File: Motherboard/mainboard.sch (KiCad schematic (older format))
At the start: 48 parts, among them IC1 BMX160, J1 Conn_01x01, J2 10118194-0001LF, J28 Conn_01x01, J29 Conn_01x01, J3 Micro_SD_Card, J30 Conn_01x01, J4 xf2m-2415-1a, J5 XF2M-1015-1A, SW1 KMR231NG LFS, U1 RFM95W-915S2, U2 ATSAMD51G_TQFN48, U4 TPS82740BSIPR, U6 MAX708RESA-T, U8 RFM95W-915S2, X1 ANTENNA_U.FL, X2 ANTENNA_U.FL

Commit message: updated PCB layout
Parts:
- C1, C2, C3, C4, C5, C7, C8: symbol Device:C_Small -> mainboard-rescue:C_Small-Device
- C10, C14: renamed from C?; value C -> 10uF; footprint (none) -> Capacitor_SMD:C_0402_1005Metric; symbol Device:C -> mainboard-rescue:C-Device
- C11, C13: renamed from C?; value C -> 2.2uF; footprint (none) -> Capacitor_SMD:C_0402_1005Metric; symbol Device:C -> mainboard-rescue:C-Device
- C12, C9: renamed from C?; value C -> 0.1uF; footprint (none) -> Capacitor_SMD:C_0402_1005Metric; symbol Device:C -> mainboard-rescue:C-Device
- D2: symbol Device:D_Schottky -> mainboard-rescue:D_Schottky-Device
- J1, J28, J29, J30: symbol Connector_Generic:Conn_01x01 -> mainboard-rescue:Conn_01x01-Connector_Generic
- L1: symbol Device:L_Small -> mainboard-rescue:L_Small-Device
- R1, R2, R3, R5: symbol Device:R_US -> mainboard-rescue:R_US-Device
- R4, R6, R7, R8: renamed from R?; symbol Device:R_US -> mainboard-rescue:R_US-Device
- U3: renamed from U?; symbol Driver_Motor:DRV8848 -> mainboard-rescue:DRV8848-Driver_Motor
- U5: renamed from U?; footprint Package_SO:TSSOP-16-1EP_4.4x5mm_P0.65mm -> KiCAD Libraries:SOP65P640X120-17N; symbol Driver_Motor:DRV8848 -> mainboard-rescue:DRV8848-Driver_Motor
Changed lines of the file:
@@
 	900  5500 1450 5500
 $Comp
-L Device:R_US R1
+L mainboard-rescue:R_US-Device R1
 U 1 1 5C3B885A
 P 900 5650
@@
 $EndComp
 $Comp
-L Device:R_US R5
+L mainboard-rescue:R_US-Device R5
 U 1 1 5C6310F9
 P 5150 7200
@@
 Connection ~ 1150 4100
 $Comp
-L Device:R_US R2
+L mainboard-rescue:R_US-Device R2
 U 1 1 5C6E5301
 P 1150 3950
@@
 SAMD51\n
 $Comp
-L Device:L_Small L1
+L mainboard-rescue:L_Small-Device L1
 U 1 1 5C59C1B4
 P 1350 4800
@@
 UHF RADIO\n
 $Comp
-L Device:C_Small C1
+L mainboard-rescue:C_Small-Device C1
 U 1 1 5DA4F94A
 P 750 6850
@@
 $EndComp
 $Comp
-L Device:C_Small C7
+L mainboard-rescue:C_Small-Device C7
 U 1 1 5DA4FC48
 P 1150 6850
@@
 Connection ~ 5700 5550
 $Comp
-L Device:D_Schottky D2
+L mainboard-rescue:D_Schottky-Device D2
 U 1 1 5D1876FB
 P 5550 4750
@@
 Connection ~ 5700 4750
 $Comp
-L Device:C_Small C2
+L mainboard-rescue:C_Small-Device C2
 U 1 1 5D1BA86A
 P 800 4800
@@
 $EndComp
 $Comp
-L Device:C_Small C5
+L mainboard-rescue:C_Small-Device C5
 U 1 1 5D1BB024
 P 1000 4800
@@
 	1000 4700 1250 4700
 $Comp
-L Device:C_Small C3
+L mainboard-rescue:C_Small-Device C3
 U 1 1 5D1C3FDB
 P 950 6850
@@
 PA07
 $Comp
-L Connector_Generic:Conn_01x01 J28
+L mainboard-rescue:Conn_01x01-Connector_Generic J28
 U 1 1 5D2A6718
 P 5000 7550
@@
 $EndComp
 $Comp
-L Connector_Generic:Conn_01x01 J1
+L mainboard-rescue:Conn_01x01-Connector_Generic J1
 U 1 1 5D2B62DF
 P 4900 7550
@@
 $EndComp
 $Comp
-L Connector_Generic:Conn_01x01 J29
+L mainboard-rescue:Conn_01x01-Connector_Generic J29
 U 1 1 5D32C3EB
 P 4800 7550
@@
 $EndComp
 $Comp
-L Connector_Generic:Conn_01x01 J30
+L mainboard-rescue:Conn_01x01-Connector_Generic J30
 U 1 1 5D338152
 P 5100 7550
@@
 $EndComp
 $Comp
-L Device:R_US R3
+L mainboard-rescue:R_US-Device R3
 U 1 1 5DAB9E18
 P 3050 1600
@@
 NoConn ~ 3300 1250
 $Comp
-L Device:C_Small C4
+L mainboard-rescue:C_Small-Device C4
 U 1 1 5DAEE375
 P 1100 1500
@@
 	1100 1600 750  1600
 $Comp
-L Device:C_Small C8
+L mainboard-rescue:C_Small-Device C8
 U 1 1 5DAF534D
 P 2700 1100
@@
 	5350 7000 5350 7350
 $Comp
-L Device:C C?
+L mainboard-rescue:C-Device C9
 U 1 1 5DB69DAC
 P 8050 900
-F 0 "C?" H 8165 946 50  0000 L CNN
-F 1 "C" H 8165 855 50  0000 L CNN
-F 2 "" H 8088 750 50  0001 C CNN
+F 0 "C9" H 8165 946 50  0000 L CNN
+F 1 "0.1uF" H 8165 855 50  0000 L CNN
+F 2 "Capacitor_SMD:C_0402_1005Metric" H 8088 750 50  0001 C CNN
 F 3 "~" H 8050 900 50  0001 C CNN
 	1    8050 900
@@
 $EndComp
 $Comp
-L Device:C C?
+L mainboard-rescue:C-Device C10
 U 1 1 5DB6B170
 P 8400 900
-F 0 "C?" H 8515 946 50  0000 L CNN
-F 1 "C" H 8515 855 50  0000 L CNN
-F 2 "" H 8438 750 50  0001 C CNN
+F 0 "C10" H 8515 946 50  0000 L CNN
+F 1 "10uF" H 8515 855 50  0000 L CNN
+F 2 "Capacitor_SMD:C_0402_1005Metric" H 8438 750 50  0001 C CNN
 F 3 "~" H 8400 900 50  0001 C CNN
 	1    8400 900
@@
 $EndComp
 $Comp
-L Device:C C?
+L mainboard-rescue:C-Device C11
 U 1 1 5DB6BC2C
 P 8150 1200
-F 0 "C?" H 8265 1246 50  0000 L CNN
-F 1 "C" H 8265 1155 50  0000 L CNN
-F 2 "" H 8188 1050 50  0001 C CNN
+F 0 "C11" H 8265 1246 50  0000 L CNN
+F 1 "2.2uF" H 8265 1155 50  0000 L CNN
+F 2 "Capacitor_SMD:C_0402_1005Metric" H 8188 1050 50  0001 C CNN
 F 3 "~" H 8150 1200 50  0001 C CNN
 	1    8150 1200
@@
 	8050 750  8400 750
 $Comp
-L power:GND #PWR?
+L power:GND #PWR0124
 U 1 1 5DBF1F8E
 P 8400 1050
-F 0 "#PWR?" H 8400 800 50  0001 C CNN
+F 0 "#PWR0124" H 8400 800 50  0001 C CNN
 F 1 "GND" H 8405 877 50  0000 C CNN
 F 2 "" H 8400 1050 50  0001 C CNN
@@
 	7500 750  8050 750
 $Comp
-L power:GND #PWR?
+L power:GND #PWR0125
 U 1 1 5DC582A1
 P 7500 2550
-F 0 "#PWR?" H 7500 2300 50  0001 C CNN
+F 0 "#PWR0125" H 7500 2300 50  0001 C CNN
 F 1 "GND" H 7505 2377 50  0000 C CNN
 F 2 "" H 7500 2550 50  0001 C CNN
@@
 MINZ_2
 $Comp
-L Driver_Motor:DRV8848 U?
+L mainboard-rescue:DRV8848-Driver_Motor U3
 U 1 1 5DB469CF
 P 7500 1850
-F 0 "U?" H 7500 2631 50  0000 C CNN
+F 0 "U3" H 7500 2631 50  0000 C CNN
 F 1 "DRV8848" H 7500 2540 50  0000 C CNN
 F 2 "Package_SO:TSSOP-16-1EP_4.4x5mm_P0.65mm" H 7500 1150 50  0001 C CNN
@@
 Connection ~ 7500 2450
 $Comp
-L power:GND #PWR?
+L power:GND #PWR0128
 U 1 1 5DCE2BBF
 P 8100 1850
-F 0 "#PWR?" H 8100 1600 50  0001 C CNN
+F 0 "#PWR0128" H 8100 1600 50  0001 C CNN
 F 1 "GND" H 8105 1677 50  0000 C CNN
 F 2 "" H 8100 1850 50  0001 C CNN
@@
 $EndComp
 $Comp
-L power:GND #PWR?
+L power:GND #PWR0129
 U 1 1 5DCE9737
 P 8100 2250
-F 0 "#PWR?" H 8100 2000 50  0001 C CNN
+F 0 "#PWR0129" H 8100 2000 50  0001 C CNN
 F 1 "GND" H 8105 2077 50  0000 C CNN
 F 2 "" H 8100 2250 50  0001 C CNN
@@
 $EndComp
 $Comp
-L Device:C C?
+L mainboard-rescue:C-Device C12
 U 1 1 5DD0AEB4
 P 9950 850
-F 0 "C?" H 10065 896 50  0000 L CNN
-F 1 "C" H 10065 805 50  0000 L CNN
-F 2 "" H 9988 700 50  0001 C CNN
+F 0 "C12" H 10065 896 50  0000 L CNN
+F 1 "0.1uF" H 10065 805 50  0000 L CNN
+F 2 "Capacitor_SMD:C_0402_1005Metric" H 9988 700 50  0001 C CNN
 F 3 "~" H 9950 850 50  0001 C CNN
 	1    9950 850
@@
 $EndComp
 $Comp
-L Device:C C?
+L mainboard-rescue:C-Device C14
 U 1 1 5DD0AEBA
 P 10300 850
-F 0 "C?" H 10415 896 50  0000 L CNN
-F 1 "C" H 10415 805 50  0000 L CNN
-F 2 "" H 10338 700 50  0001 C CNN
+F 0 "C14" H 10415 896 50  0000 L CNN
+F 1 "10uF" H 10415 805 50  0000 L CNN
+F 2 "Capacitor_SMD:C_0402_1005Metric" H 10338 700 50  0001 C CNN
 F 3 "~" H 10300 850 50  0001 C CNN
 	1    10300 850
@@
 $EndComp
 $Comp
-L Device:C C?
+L mainboard-rescue:C-Device C13
 U 1 1 5DD0AEC0
 P 10050 1150
-F 0 "C?" H 10165 1196 50  0000 L CNN
-F 1 "C" H 10165 1105 50  0000 L CNN
-F 2 "" H 10088 1000 50  0001 C CNN
+F 0 "C13" H 10165 1196 50  0000 L CNN
+F 1 "2.2uF" H 10165 1105 50  0000 L CNN
+F 2 "Capacitor_SMD:C_0402_1005Metric" H 10088 1000 50  0001 C CNN
 F 3 "~" H 10050 1150 50  0001 C CNN
 	1    10050 1150
@@
 	9950 700  10300 700
 $Comp
-L power:GND #PWR?
+L power:GND #PWR0130
 U 1 1 5DD0AEC8
 P 10300 1000
-F 0 "#PWR?" H 10300 750 50  0001 C CNN
+F 0 "#PWR0130" H 10300 750 50  0001 C CNN
 F 1 "GND" H 10305 827 50  0000 C CNN
 F 2 "" H 10300 1000 50  0001 C CNN
@@
 	9400 700  9950 700
 $Comp
-L power:GND #PWR?
+L power:GND #PWR0131
 U 1 1 5DD0AED6
 P 9400 2500
-F 0 "#PWR?" H 9400 2250 50  0001 C CNN
+F 0 "#PWR0131" H 9400 2250 50  0001 C CNN
 F 1 "GND" H 9405 2327 50  0000 C CNN
 F 2 "" H 9400 2500 50  0001 C CNN
@@
 MINZ_2
 $Comp
-L Driver_Motor:DRV8848 U?
+L mainboard-rescue:DRV8848-Driver_Motor U5
 U 1 1 5DD0AEE3
 P 9400 1800
-F 0 "U?" H 9400 2581 50  0000 C CNN
+F 0 "U5" H 9400 2581 50  0000 C CNN
 F 1 "DRV8848" H 9400 2490 50  0000 C CNN
-F 2 "Package_SO:TSSOP-16-1EP_4.4x5mm_P0.65mm" H 9400 1100 50  0001 C CNN
+F 2 "KiCAD Libraries:SOP65P640X120-17N" H 9400 1100 50  0001 C CNN
 F 3 "http://www.ti.com/lit/ds/symlink/drv8848.pdf" H 8250 3150 50  0001 C CNN
 	1    9400 1800
@@
 Connection ~ 9400 2400
 $Comp
-L power:GND #PWR?
+L power:GND #PWR0132
 U 1 1 5DD0AEF2
 P 10000 1800
-F 0 "#PWR?" H 10000 1550 50  0001 C CNN
+F 0 "#PWR0132" H 10000 1550 50  0001 C CNN
 F 1 "GND" H 10005 1627 50  0000 C CNN
 F 2 "" H 10000 1800 50  0001 C CNN
@@
 	10000 1850 10000 1800
 $Comp
-L power:GND #PWR?
+L power:GND #PWR0133
 U 1 1 5DD0AEF9
 P 10000 2200
-F 0 "#PWR?" H 10000 1950 50  0001 C CNN
+F 0 "#PWR0133" H 10000 1950 50  0001 C CNN
 F 1 "GND" H 10005 2027 50  0000 C CNN
 F 2 "" H 10000 2200 50  0001 C CNN
@@
 	4550 6200 4450 6200
 $Comp
-L Device:R_US R?
+L mainboard-rescue:R_US-Device R4
 U 1 1 5DB0C8A9
 P 4500 3950
-F 0 "R?" H 4600 3750 50  0000 C CNN
+F 0 "R4" H 4600 3750 50  0000 C CNN
 F 1 "10K" H 4600 3850 50  0000 C CNN
 F 2 "Resistor_SMD:R_0402_1005Metric" V 4540 3940 50  0001 C CNN
@@
 	4500 4100 4450 4100
 $Comp
-L Device:R_US R?
+L mainboard-rescue:R_US-Device R6
 U 1 1 5DB0D4A3
 P 4650 3850
-F 0 "R?" H 4550 3800 50  0000 C CNN
+F 0 "R6" H 4550 3800 50  0000 C CNN
 F 1 "10K" H 4550 3900 50  0000 C CNN
 F 2 "Resistor_SMD:R_0402_1005Metric" V 4690 3840 50  0001 C CNN
@@
 	4650 4000 4700 4000
 $Comp
-L power:+3V3 #PWR?
+L power:+3V3 #PWR0134
 U 1 1 5DB0E5CD
 P 4650 3600
-F 0 "#PWR?" H 4650 3450 50  0001 C CNN
+F 0 "#PWR0134" H 4650 3450 50  0001 C CNN
 F 1 "+3V3" H 4665 3773 50  0000 C CNN
 F 2 "" H 4650 3600 50  0001 C CNN
@@
 NoConn ~ 1150 2200
 $Comp
-L Device:R_US R?
+L mainboard-rescue:R_US-Device R7
 U 1 1 5DB33981
 P 5100 5750
-F 0 "R?" H 5200 5550 50  0000 C CNN
+F 0 "R7" H 5200 5550 50  0000 C CNN
 F 1 "10K" H 5200 5650 50  0000 C CNN
 F 2 "Resistor_SMD:R_0402_1005Metric" V 5140 5740 50  0001 C CNN
@@
 $EndComp
 $Comp
-L Device:R_US R?
+L mainboard-rescue:R_US-Device R8
 U 1 1 5DB33987
 P 5250 5650
-F 0 "R?" H 5150 5600 50  0000 C CNN
+F 0 "R8" H 5150 5600 50  0000 C CNN
 F 1 "10K" H 5150 5700 50  0000 C CNN
 F 2 "Resistor_SMD:R_0402_1005Metric" V 5290 5640 50  0001 C CNN
@@
 $EndComp
 $Comp
-L power:+3V3 #PWR?
+L power:+3V3 #PWR0135
 U 1 1 5DB3398D
 P 5250 5400
-F 0 "#PWR?" H 5250 5250 50  0001 C CNN
+F 0 "#PWR0135" H 5250 5250 50  0001 C CNN
 F 1 "+3V3" H 5265 5573 50  0000 C CNN
 F 2 "" H 5250 5400 50  0001 C CNN

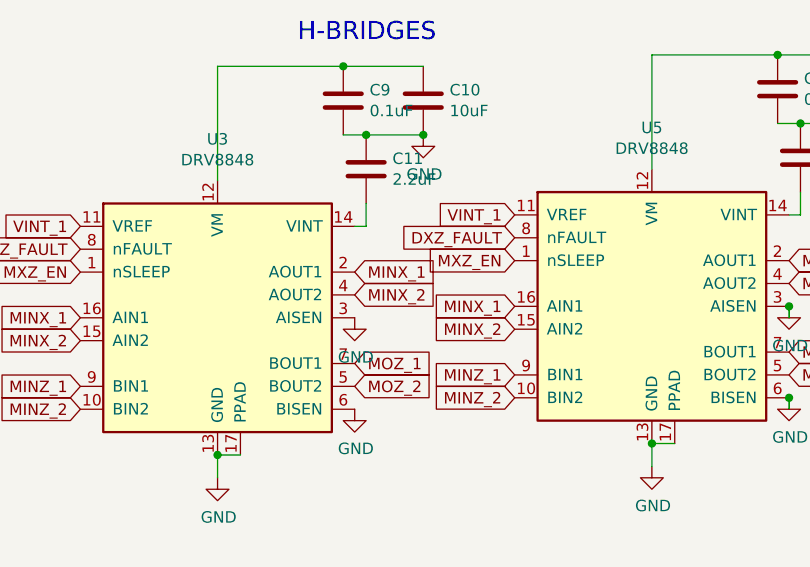
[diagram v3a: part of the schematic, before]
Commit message: updated H-bridge nets on schematic
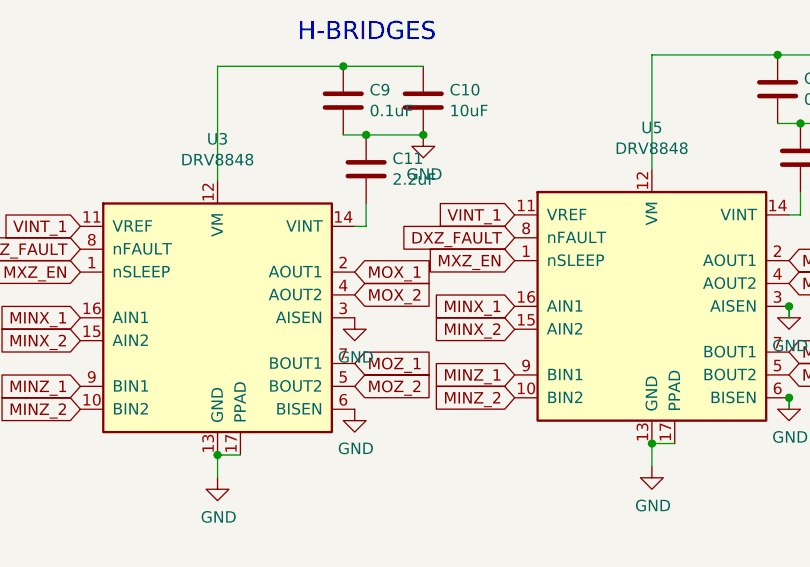
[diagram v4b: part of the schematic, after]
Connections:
- net MINX_1: no longer U3.2 (AOUT1)
- net MINX_2: no longer U3.4 (AOUT2)
- new net MOX_1: U3.2 (AOUT1)
- new net MOX_2: U3.4 (AOUT2)
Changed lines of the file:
@@
 $EndComp
 Text GLabel 8100 1650 2    50   Input ~ 0
-MINX_1
+MOX_1
 Text GLabel 8100 1750 2    50   Input ~ 0
-MINX_2
+MOX_2
 Text GLabel 8100 2050 2    50   Input ~ 0
 MOZ_1

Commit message: updated H-bridge footprints with footprints from component search engine
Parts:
- U3: footprint Package_SO:TSSOP-16-1EP_4.4x5mm_P0.65mm -> KiCAD Libraries:SOP65P640X120-17N
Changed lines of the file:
@@
 F 0 "U3" H 7500 2631 50  0000 C CNN
 F 1 "DRV8848" H 7500 2540 50  0000 C CNN
-F 2 "Package_SO:TSSOP-16-1EP_4.4x5mm_P0.65mm" H 7500 1150 50  0001 C CNN
+F 2 "KiCAD Libraries:SOP65P640X120-17N" H 7500 1150 50  0001 C CNN
 F 3 "http://www.ti.com/lit/ds/symlink/drv8848.pdf" H 6350 3200 50  0001 C CNN
 	1    7500 1850

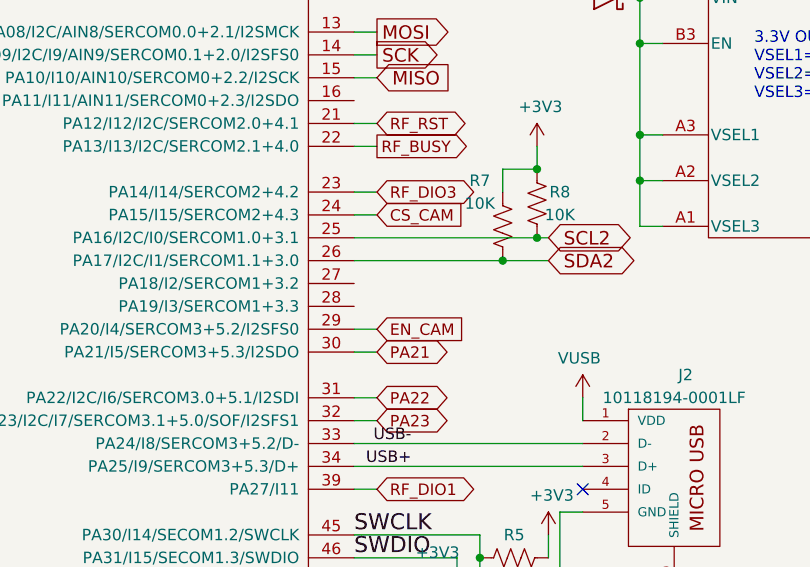
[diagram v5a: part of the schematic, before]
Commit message: updated wiring on top layer, added CS_IMU net
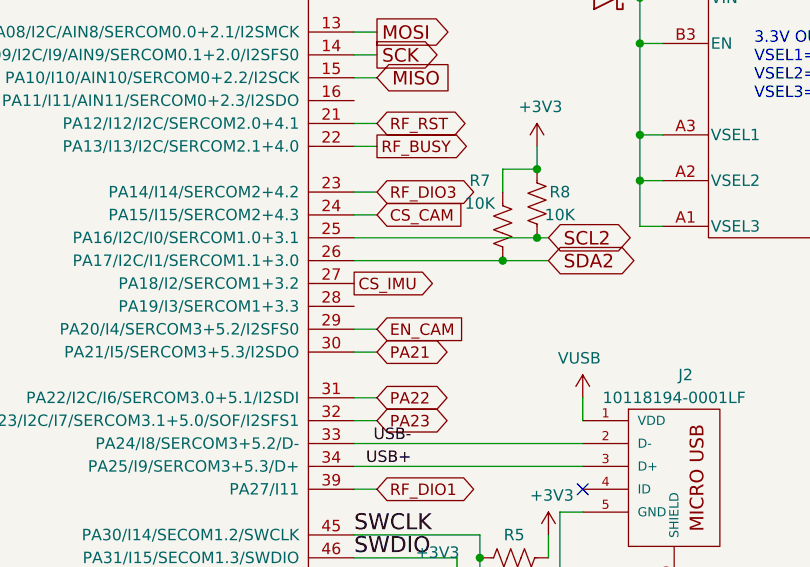
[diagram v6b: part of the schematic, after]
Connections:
- net CS_IMU: now also U2.27 (PA18/I2/SERCOM1+3.2)
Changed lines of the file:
@@
 Wire Wire Line
 	5250 5800 5300 5800
+Text GLabel 4450 6000 2    50   Output ~ 0
+CS_IMU
 $EndSCHEMATC

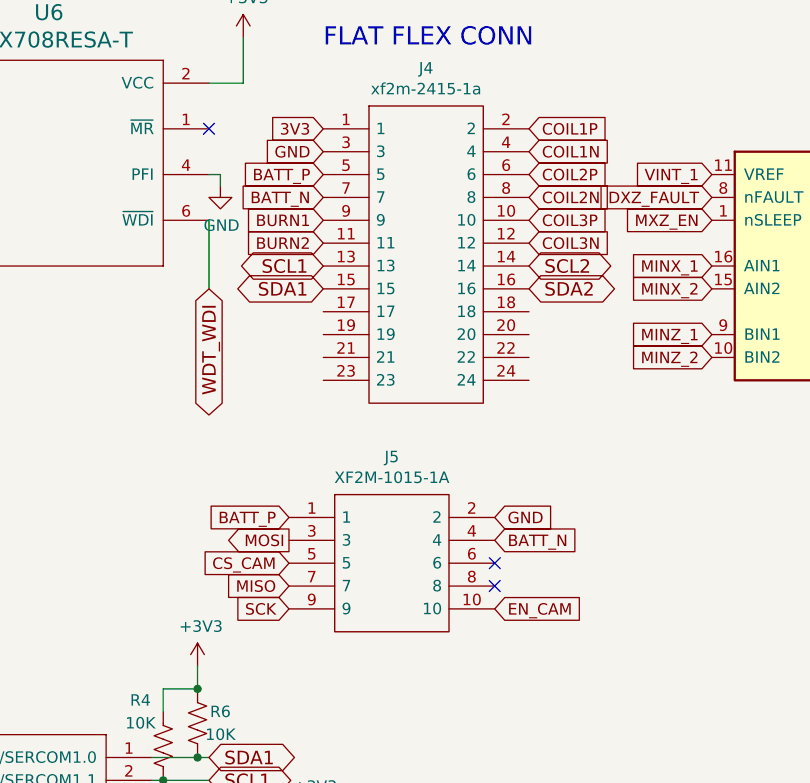
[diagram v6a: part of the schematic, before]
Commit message: updated camera connector and connected to MCU and flat flex connector
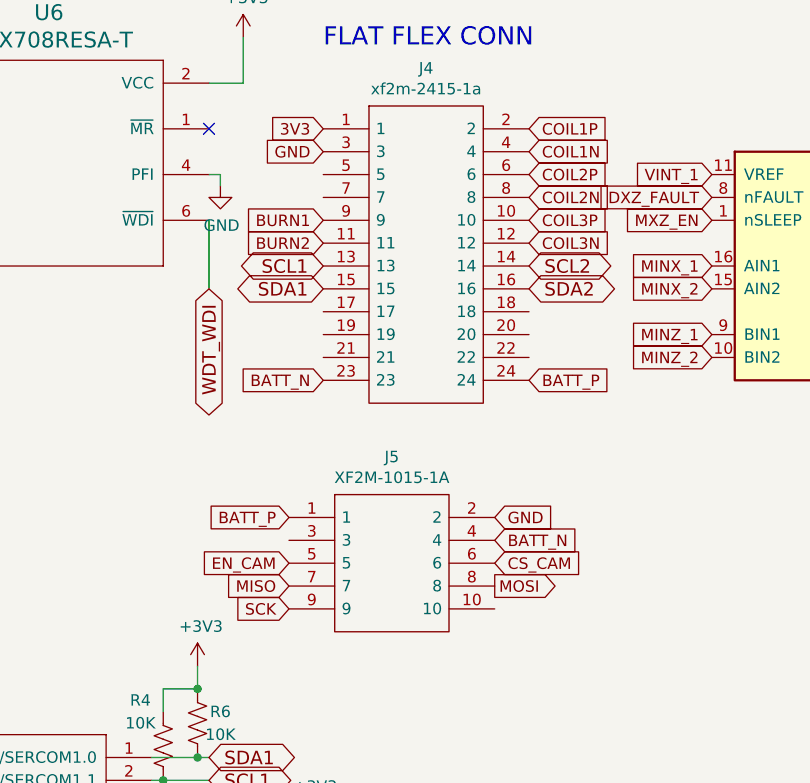
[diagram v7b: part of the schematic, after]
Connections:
- net BATT_N: now also J4.23; no longer J4.7
- net BATT_P: now also J4.24; no longer J4.5
- net CS_CAM: now also J5.6; no longer J5.5
- net EN_CAM: now also J5.5; no longer J5.10
- net MOSI: now also J5.8; no longer J5.3
- no-connect marks 12 -> 10

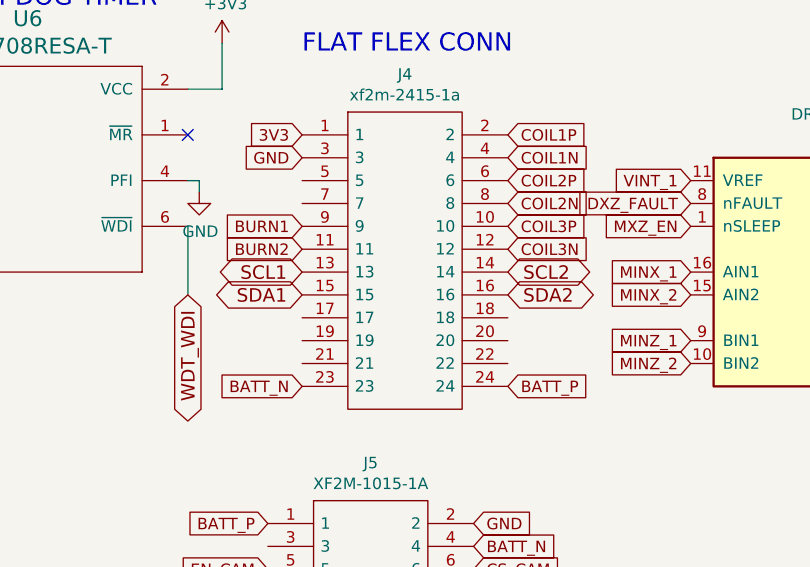
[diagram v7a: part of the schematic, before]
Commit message: added WDT_WDI net to MCU, connected C2, C5, and L1 to MCU
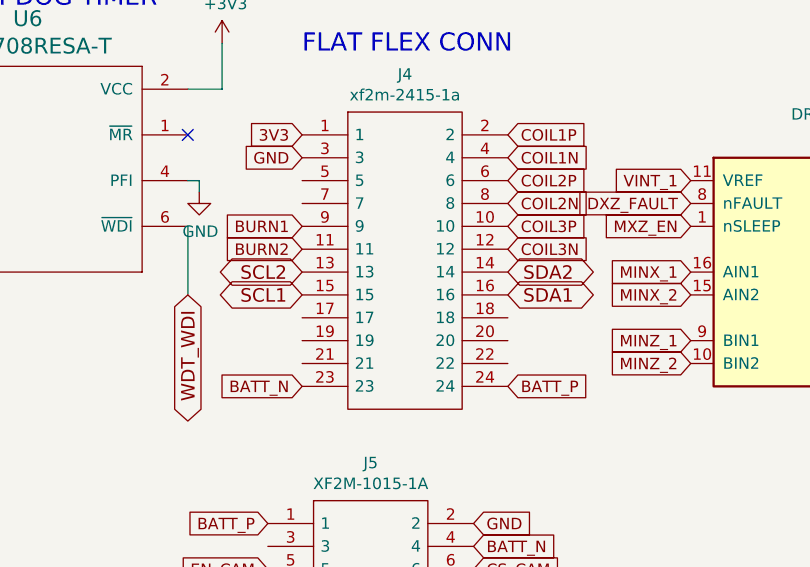
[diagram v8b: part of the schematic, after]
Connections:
- net SCL1: now also J4.15; no longer J4.13
- net SCL2: now also J4.13; no longer J4.14
- net SDA1: now also J4.16; no longer J4.15
- net SDA2: now also J4.14; no longer J4.16
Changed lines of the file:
@@
 Text Notes 2600 7900 0    50   ~ 0
 I2C_1\nSCL: PA01\nSDA: PA00\n\nI2C_2\nSCL: PA16\nSDA: PA17\n
+Text GLabel 6100 1950 2    59   BiDi ~ 0
+SDA1
 Text GLabel 5200 1950 0    59   BiDi ~ 0
-SDA1
+SCL1
 Text GLabel 5200 1850 0    59   BiDi ~ 0
-SCL1
+SCL2
 Text GLabel 6100 1850 2    59   BiDi ~ 0
-SCL2
-Text GLabel 6100 1950 2    59   BiDi ~ 0
 SDA2
 Wire Wire Line
